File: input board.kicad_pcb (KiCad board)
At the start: 2 copper layers, 149.9 x 148.6 mm, 78 parts, among them J1 Conn_01x05_Female, J10 Conn_01x05_Female, J11 Conn_01x04_Female, J12 MCU_LEFT_LEGS, J13 MCU_RIGHT_LEGS, J2 Conn_01x05_Female, J3 Conn_01x05_Female, J4 Conn_01x05_Female, J5 Conn_01x05_Female, J6 Conn_01x05_Female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

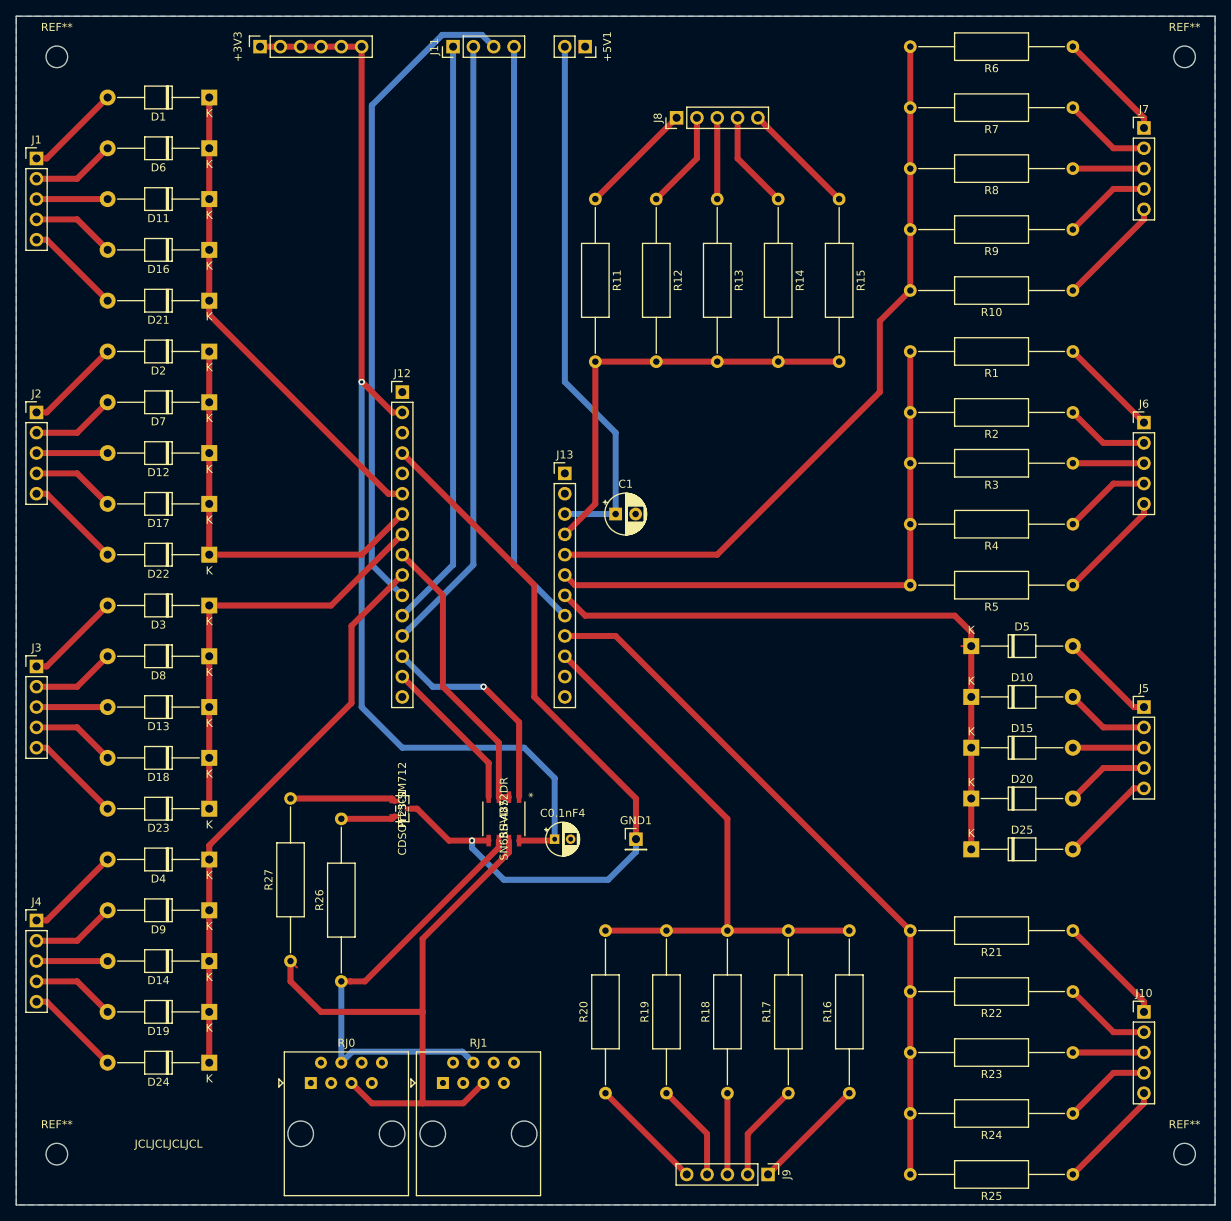
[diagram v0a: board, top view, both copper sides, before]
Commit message: Update mounting holes and ground plane
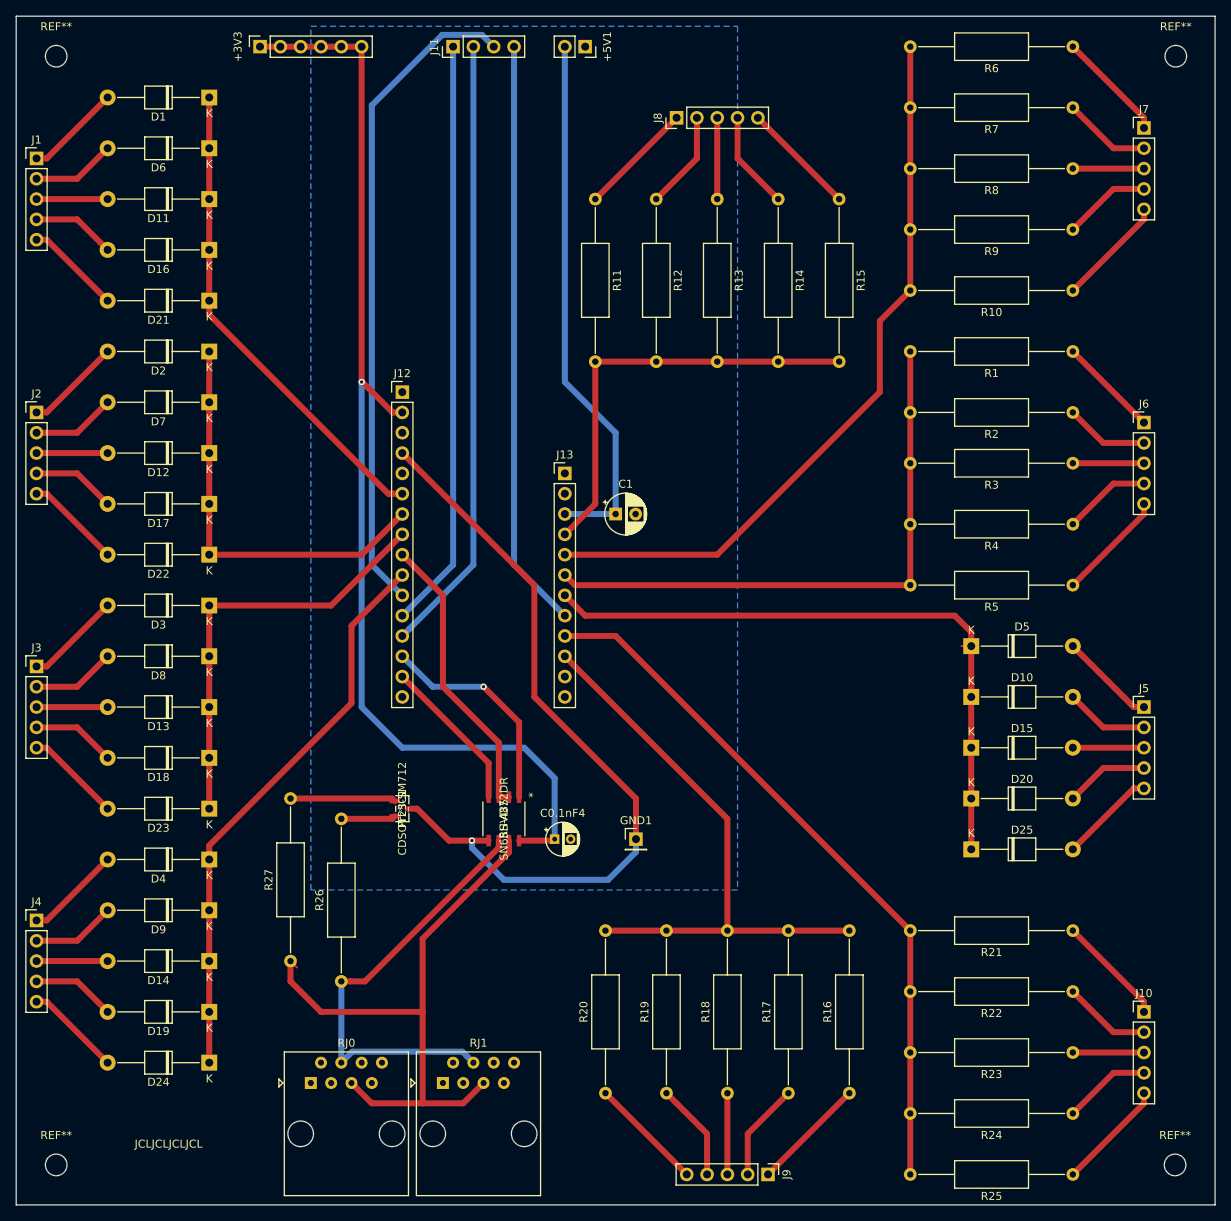
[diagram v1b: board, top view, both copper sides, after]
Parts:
- moved REF** 1.80 mm to (202.0, 161.4)
- moved REF** 1.35 mm to (62.1, 161.4)
- moved REF** 1.10 mm to (202.1, 22.8)
- moved REF** 0.11 mm to (62.1, 22.8)
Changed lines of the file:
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@@
   )
   (module MountingHole:MountingHole_2.7mm_M2.5 (layer F.Cu)
-    (at 203.2 22.86)
+    (at 202.1 22.78)
     (descr "Mounting Hole 2.7mm, no annular, M2.5")
     (tags "mounting hole 2.7mm no annular m2.5")
@@
   )
   (module MountingHole:MountingHole_2.7mm_M2.5 (layer F.Cu)
-    (at 203.2 160.02)
+    (at 202.01 161.37)
     (descr "Mounting Hole 2.7mm, no annular, M2.5")
     (tags "mounting hole 2.7mm no annular m2.5")
@@
   )
   (module MountingHole:MountingHole_2.7mm_M2.5 (layer F.Cu)
-    (at 62.23 160.02)
+    (at 62.15 161.37)
     (descr "Mounting Hole 2.7mm, no annular, M2.5")
     (tags "mounting hole 2.7mm no annular m2.5")
@@
   )
   (module MountingHole:MountingHole_2.7mm_M2.5 (layer F.Cu)
-    (at 62.23 22.86)
+    (at 62.15 22.78)
     (descr "Mounting Hole 2.7mm, no annular, M2.5")
     (tags "mounting hole 2.7mm no annular m2.5")
@@
     (polygon
       (pts
-        (xy 207.01 166.37) (xy 57.15 166.37) (xy 57.15 17.78) (xy 207.01 17.78)
+        (xy 147.32 127) (xy 93.98 127) (xy 93.98 19.05) (xy 147.32 19.05)
       )
     )

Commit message: Updated PCB and gbr files
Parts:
- removed R10, R11, R12, R13, R14, R15, R16, R17, R18, R19, R20, R21, R22, R23, R24, R25, R9: 220, Resistor_THT:R_Axial_DIN0309_L9.0mm_D3.2mm_P20.32mm_Horizontal
- removed the R6 at (189.2, 21.6)
- removed the R7 at (189.2, 29.2)
- added D26: LED, LED_THT:LED_D5.0mm, F.Cu at (74.9, 22.9)
- R1, R2, R3, R4, R5: value 220 -> 10k
- R8: value 220 -> 470
- moved J10 144.6 mm to (64.8, 86.4)
- moved J6 137.1 mm to (64.8, 36.8)
- moved J7 135.1 mm to (64.8, 53.3)
- moved J1 134.9 mm to (184.2, 87.6)
- moved D14 129.3 mm to (156.2, 30.5), turned to 270 degrees
- moved D16 128.6 mm to (154.9, 152.4), turned to 90 degrees
- moved J2 125.0 mm to (184.2, 55.9)
- moved R4 122.6 mm to (68.6, 102.9), turned to 0 degrees
- moved R1 122.0 mm to (68.6, 41.9), turned to 0 degrees
- moved R2 121.2 mm to (68.6, 55.9), turned to 0 degrees
- moved R3 120.7 mm to (68.6, 72.4), turned to 0 degrees
- moved R5 120.6 mm to (68.6, 88.9), turned to 0 degrees
- moved J3 115.9 mm to (144.8, 20.3), turned to 90 degrees
- moved R8 112.0 mm to (77.5, 29.2), turned to 0 degrees
- moved D9 111.7 mm to (174.0, 67.3)
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- renumbered R26 to R6, R27 to R7
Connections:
- D1 pad 1: /A1 -> Net-(D1-Pad1)
- D1 pad 2: /101 -> /D11
- D10 pad 1: /D10 -> Net-(D10-Pad1)
- D10 pad 2: /205 -> /D12
- D11 pad 1: /A1 -> Net-(D11-Pad1)
- D11 pad 2: /301 -> /D13
- D12 pad 1: /A2 -> Net-(D12-Pad1)
- D12 pad 2: /302 -> /D13
- D13 pad 1: /A3 -> Net-(D13-Pad1)
- D13 pad 2: /303 -> /D13
- D14 pad 1: /A5 -> Net-(D14-Pad1)
- D14 pad 2: /304 -> /D13
- D15 pad 1: /D10 -> Net-(D15-Pad1)
- D15 pad 2: /305 -> /D13
- D16 pad 1: /A1 -> Net-(D16-Pad1)
- D16 pad 2: /401 -> /D5
- D17 pad 1: /A2 -> Net-(D17-Pad1)
- D17 pad 2: /402 -> /D5
- D18 pad 1: /A3 -> Net-(D18-Pad1)
- D18 pad 2: /403 -> /D5
- D19 pad 1: /A5 -> Net-(D19-Pad1)
- D19 pad 2: /404 -> /D5
- D2 pad 1: /A2 -> Net-(D2-Pad1)
- D2 pad 2: /102 -> /D11
- D20 pad 1: /D10 -> Net-(D20-Pad1)
- D20 pad 2: /405 -> /D5
- D21 pad 1: /A1 -> Net-(D21-Pad1)
- D21 pad 2: /501 -> /D6
- D22 pad 1: /A2 -> Net-(D22-Pad1)
- D22 pad 2: /502 -> /D6
- D23 pad 1: /A3 -> Net-(D23-Pad1)
- D23 pad 2: /503 -> /D6
- D24 pad 1: /A5 -> Net-(D24-Pad1)
- D24 pad 2: /504 -> /D6
- D25 pad 1: /D10 -> Net-(D25-Pad1)
- D25 pad 2: /505 -> /D6
- D3 pad 1: /A3 -> Net-(D3-Pad1)
- D3 pad 2: /103 -> /D11
- D4 pad 1: /A5 -> Net-(D4-Pad1)
- D4 pad 2: /104 -> /D11
- D5 pad 1: /D10 -> Net-(D5-Pad1)
- D5 pad 2: /105 -> /D11
- D6 pad 1: /A1 -> Net-(D6-Pad1)
- D6 pad 2: /201 -> /D12
- D7 pad 1: /A2 -> Net-(D7-Pad1)
- D7 pad 2: /202 -> /D12
- D8 pad 1: /A3 -> Net-(D8-Pad1)
- D8 pad 2: /203 -> /D12
- D9 pad 1: /A5 -> Net-(D9-Pad1)
- D9 pad 2: /204 -> /D12
- J1 pad 1: /101 -> Net-(D1-Pad1)
- J1 pad 2: /201 -> Net-(D2-Pad1)
- J1 pad 3: /301 -> Net-(D3-Pad1)
- J1 pad 4: /401 -> Net-(D4-Pad1)
- J1 pad 5: /501 -> Net-(D5-Pad1)
- J10 pad 1: /501 -> /A5
- J10 pad 2: /502 -> /A5
- J10 pad 3: /503 -> /A5
- J10 pad 4: /504 -> /A5
- J10 pad 5: /505 -> /A5
- J2 pad 1: /102 -> Net-(D6-Pad1)
- J2 pad 2: /202 -> Net-(D7-Pad1)
- J2 pad 3: /302 -> Net-(D8-Pad1)
- J2 pad 4: /402 -> Net-(D9-Pad1)
- J2 pad 5: /502 -> Net-(D10-Pad1)
- J3 pad 1: /103 -> Net-(D11-Pad1)
- J3 pad 2: /203 -> Net-(D12-Pad1)
- J3 pad 3: /303 -> Net-(D13-Pad1)
- J3 pad 4: /403 -> Net-(D14-Pad1)
- J3 pad 5: /503 -> Net-(D15-Pad1)
- J4 pad 1: /104 -> Net-(D16-Pad1)
- J4 pad 2: /204 -> Net-(D17-Pad1)
- J4 pad 3: /304 -> Net-(D18-Pad1)
- J4 pad 4: /404 -> Net-(D19-Pad1)
- J4 pad 5: /504 -> Net-(D20-Pad1)
- J5 pad 1: /105 -> Net-(D21-Pad1)
- J5 pad 2: /205 -> Net-(D22-Pad1)
- J5 pad 3: /305 -> Net-(D23-Pad1)
- J5 pad 4: /405 -> Net-(D24-Pad1)
- J5 pad 5: /505 -> Net-(D25-Pad1)
- J6 pad 1: /101 -> /A1
- J6 pad 2: /102 -> /A1
- J6 pad 3: /103 -> /A1
- J6 pad 4: /104 -> /A1
- J6 pad 5: /105 -> /A1
- J7 pad 1: /201 -> /A2
- J7 pad 2: /202 -> /A2
- J7 pad 3: /203 -> /A2
- J7 pad 4: /204 -> /A2
- J7 pad 5: /205 -> /A2
- J8 pad 1: /301 -> /A3
- J8 pad 2: /302 -> /A3
- J8 pad 3: /303 -> /A3
- J8 pad 4: /304 -> /A3
- J8 pad 5: /305 -> /A3
- J9 pad 1: /401 -> /D10
- J9 pad 2: /402 -> /D10
- J9 pad 3: /403 -> /D10
- J9 pad 4: /404 -> /D10
- J9 pad 5: /405 -> /D10
- R1 pad 1: /101 -> /A1
- R1 pad 2: /D11 -> +3V3
- R2 pad 1: /102 -> /A2
- R2 pad 2: /D11 -> +3V3
- R3 pad 1: /103 -> /A3
- R3 pad 2: /D11 -> +3V3
- R4 pad 1: /104 -> /D10
- R4 pad 2: /D11 -> +3V3
- R5 pad 1: /105 -> /A5
- R5 pad 2: /D11 -> +3V3
- R8 pad 1: /203 -> Net-(D26-Pad2)
- R8 pad 2: /D12 -> +3V3
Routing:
- net +3V3: track 141.8 -> 216.0 mm
- net /D10: track 81.1 -> 153.8 mm
- net /D12: track 92.5 -> 65.7 mm
- net /105: track 25.9 -> 0.00 mm
- net /505: track 25.9 -> 0.00 mm
- net /501: track 25.9 -> 0.00 mm
- net /405: track 24.8 -> 0.00 mm
- net /401: track 24.8 -> 0.00 mm
- net /101: track 24.6 -> 0.00 mm
- net /205: track 24.3 -> 0.00 mm
- net /201: track 24.3 -> 0.00 mm
- net /305: track 23.3 -> 0.00 mm
- net /301: track 23.3 -> 0.00 mm
- net /502: track 23.0 -> 0.00 mm
- net /104: track 23.0 -> 0.00 mm
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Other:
- board size 149.9 x 148.6 mm -> 124.5 x 148.6 mm
